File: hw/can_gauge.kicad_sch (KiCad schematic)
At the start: 9 parts, among them U2 MCP2515-xP

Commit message: hw: power and ground
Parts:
- removed U2: MCP2515-xP, symbol CAN:MCP2515-xP
- added C3, C4: 0.1 uF, symbol Device:C_Small
- added U1: MCP2515-xSO, Package_DIP:DIP-18_W7.62mm, symbol Interface_CAN_LIN:MCP2515-xSO
- renumbered Vreg to Vreg1
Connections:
- net +5V: now also UC1.1 (VDD), C3.1, C4.1, U1.18 (VDD)
- net GND: now also UC1.20 (VSS), C3.2, C4.2, U1.9 (VSS)
- net TX: now reaches XCVR1.1 (TXD)
- net TX: now also U1.1 (TXCAN)
- net RX: now reaches XCVR1.4 (RXD)
- net RX: now also U1.2 (RXCAN)
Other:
- moved on the sheet: UC1

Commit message: hw: mcp2515 serial lines
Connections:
- net at UC1.10 (RB7): now also U1.15 (SO)
- net at UC1.11 (RB6): now also U1.16 (~{CS})
- net at UC1.12 (RB5): now also U1.13 (SCK)
- net at UC1.13 (RB4): now also U1.14 (SI)
- net INT: now reaches UC1.17 (RA2)
- net INT: now also U1.12 (~{INT})
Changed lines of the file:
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@@
+	(wire
+		(pts
+			(xy 185.42 68.58) (xy 184.15 68.58)
+		)
+		(stroke
+			(width 0)
+			(type default)
+		)
+	)
 	(wire
 		(pts
@@
 	(wire
 		(pts
+			(xy 77.47 55.88) (xy 88.9 55.88)
+		)
+		(stroke
+			(width 0)
+			(type default)
+		)
+	)
+	(wire
+		(pts
 			(xy 232.41 36.83) (xy 236.22 36.83)
 		)
@@
 	(wire
 		(pts
+			(xy 77.47 99.06) (xy 77.47 55.88)
+		)
+		(stroke
+			(width 0)
+			(type default)
+		)
+	)
+	(wire
+		(pts
 			(xy 238.76 52.07) (xy 245.11 52.07)
 		)
@@
 	(wire
 		(pts
+			(xy 137.16 99.06) (xy 77.47 99.06)
+		)
+		(stroke
+			(width 0)
+			(type default)
+		)
+	)
+	(wire
+		(pts
 			(xy 104.14 31.75) (xy 104.14 38.1)
 		)
@@
 	(wire
 		(pts
+			(xy 153.67 60.96) (xy 137.16 60.96)
+		)
+		(stroke
+			(width 0)
+			(type default)
+		)
+	)
+	(wire
+		(pts
+			(xy 82.55 21.59) (xy 82.55 53.34)
+		)
+		(stroke
+			(width 0)
+			(type default)
+		)
+	)
+	(wire
+		(pts
 			(xy 177.8 39.37) (xy 181.61 39.37)
 		)
@@
 	(wire
 		(pts
+			(xy 153.67 55.88) (xy 132.08 55.88)
+		)
+		(stroke
+			(width 0)
+			(type default)
+		)
+	)
+	(wire
+		(pts
 			(xy 245.11 57.15) (xy 252.73 57.15)
 		)
@@
 	(wire
 		(pts
+			(xy 134.62 58.42) (xy 134.62 96.52)
+		)
+		(stroke
+			(width 0)
+			(type default)
+		)
+	)
+	(wire
+		(pts
 			(xy 236.22 59.69) (xy 238.76 59.69)
 		)
@@
 	(wire
 		(pts
+			(xy 132.08 93.98) (xy 82.55 93.98)
+		)
+		(stroke
+			(width 0)
+			(type default)
+		)
+	)
+	(wire
+		(pts
+			(xy 82.55 53.34) (xy 88.9 53.34)
+		)
+		(stroke
+			(width 0)
+			(type default)
+		)
+	)
+	(wire
+		(pts
 			(xy 113.03 38.1) (xy 118.11 38.1)
 		)
@@
 	(wire
 		(pts
+			(xy 153.67 53.34) (xy 132.08 53.34)
+		)
+		(stroke
+			(width 0)
+			(type default)
+		)
+	)
+	(wire
+		(pts
+			(xy 82.55 60.96) (xy 88.9 60.96)
+		)
+		(stroke
+			(width 0)
+			(type default)
+		)
+	)
+	(wire
+		(pts
+			(xy 82.55 93.98) (xy 82.55 60.96)
+		)
+		(stroke
+			(width 0)
+			(type default)
+		)
+	)
+	(wire
+		(pts
+			(xy 80.01 96.52) (xy 80.01 58.42)
+		)
+		(stroke
+			(width 0)
+			(type default)
+		)
+	)
+	(wire
+		(pts
+			(xy 132.08 21.59) (xy 82.55 21.59)
+		)
+		(stroke
+			(width 0)
+			(type default)
+		)
+	)
+	(wire
+		(pts
 			(xy 168.91 39.37) (xy 168.91 48.26)
 		)
@@
 	(wire
 		(pts
+			(xy 153.67 58.42) (xy 134.62 58.42)
+		)
+		(stroke
+			(width 0)
+			(type default)
+		)
+	)
+	(wire
+		(pts
 			(xy 208.28 62.23) (xy 210.82 62.23)
 		)
@@
 	(wire
 		(pts
+			(xy 132.08 53.34) (xy 132.08 21.59)
+		)
+		(stroke
+			(width 0)
+			(type default)
+		)
+	)
+	(wire
+		(pts
 			(xy 245.11 62.23) (xy 270.51 62.23)
 		)
@@
 	(wire
 		(pts
+			(xy 132.08 55.88) (xy 132.08 93.98)
+		)
+		(stroke
+			(width 0)
+			(type default)
+		)
+	)
+	(wire
+		(pts
 			(xy 238.76 62.23) (xy 245.11 62.23)
 		)
@@
 	(wire
 		(pts
+			(xy 134.62 96.52) (xy 80.01 96.52)
+		)
+		(stroke
+			(width 0)
+			(type default)
+		)
+	)
+	(wire
+		(pts
 			(xy 223.52 33.02) (xy 223.52 36.83)
 		)
@@
 		(pts
 			(xy 104.14 38.1) (xy 107.95 38.1)
+		)
+		(stroke
+			(width 0)
+			(type default)
+		)
+	)
+	(wire
+		(pts
+			(xy 80.01 58.42) (xy 88.9 58.42)
+		)
+		(stroke
+			(width 0)
+			(type default)
+		)
+	)
+	(wire
+		(pts
+			(xy 137.16 60.96) (xy 137.16 99.06)
 		)
 		(stroke
@@
 		)
 	)
+	(global_label "INT"
+		(shape input)
+		(at 88.9 71.12 180)
+		(fields_autoplaced yes)
+		(effects
+			(font
+				(size 1.27 1.27)
+			)
+			(justify right)
+		)
+		(property "Intersheetrefs" "${INTERSHEET_REFS}"
+			(at 83.0119 71.12 0)
+			(effects
+				(font
+					(size 1.27 1.27)
+				)
+				(justify right)
+				(hide yes)
+			)
+		)
+	)
 	(global_label "RX"
 		(shape input)
@@
 			(effects
 				(font
+					(size 1.27 1.27)
+				)
+				(justify left)
+				(hide yes)
+			)
+		)
+	)
+	(global_label "INT"
+		(shape output)
+		(at 185.42 68.58 0)
+		(fields_autoplaced yes)
+		(effects
+			(font
+				(size 1.27 1.27)
+			)
+			(justify left)
+		)
+		(property "Intersheetrefs" "${INTERSHEET_REFS}"
+			(at 191.3081 68.58 0)
+			(effects
+				(font

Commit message: hw: mcp2515 reset
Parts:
- added R4: 10k, symbol Device:R_Small_US
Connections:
- net +5V: now also R4.2
- net at U1.17 (~{RESET}): now also R4.1
- no-connect marks 0 -> 5
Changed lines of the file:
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@@
 		(color 0 0 0 0)
 	)
+	(no_connect
+		(at 184.15 76.2)
+	)
+	(no_connect
+		(at 184.15 81.28)
+	)
+	(no_connect
+		(at 184.15 73.66)
+	)
+	(no_connect
+		(at 184.15 71.12)
+	)
+	(no_connect
+		(at 184.15 78.74)
+	)
 	(wire
 		(pts
@@
 	(wire
 		(pts
+			(xy 195.58 83.82) (xy 195.58 82.55)
+		)
+		(stroke
+			(width 0)
+			(type default)
+		)
+	)
+	(wire
+		(pts
 			(xy 236.22 54.61) (xy 238.76 54.61)
 		)
@@
 	(wire
 		(pts
+			(xy 191.77 83.82) (xy 195.58 83.82)
+		)
+		(stroke
+			(width 0)
+			(type default)
+		)
+	)
+	(wire
+		(pts
 			(xy 245.11 62.23) (xy 270.51 62.23)
 		)
@@
 		(pts
 			(xy 104.14 38.1) (xy 104.14 48.26)
+		)
+		(stroke
+			(width 0)
+			(type default)
+		)
+	)
+	(wire
+		(pts
+			(xy 184.15 83.82) (xy 186.69 83.82)
 		)
 		(stroke
@@
 	)
 	(symbol
+		(lib_id "Device:R_Small_US")
+		(at 189.23 83.82 90)
+		(unit 1)
+		(exclude_from_sim no)
+		(in_bom yes)
+		(on_board yes)
+		(dnp no)
+		(fields_autoplaced yes)
+		(property "Reference" "R4"
+			(at 189.23 77.47 90)
+			(effects
+				(font
+					(size 1.27 1.27)
+				)
+			)
+		)
+		(property "Value" "10k"
+			(at 189.23 80.01 90)
+			(effects
+				(font
+					(size 1.27 1.27)
+				)
+			)
+		)
+		(property "Footprint" ""
+			(at 189.23 83.82 0)
+			(effects
+				(font
+					(size 1.27 1.27)
+				)
+				(hide yes)
+			)
+		)
+		(property "Datasheet" "~"
+			(at 189.23 83.82 0)
+			(effects
+				(font
+					(size 1.27 1.27)
+				)
+				(hide yes)
+			)
+		)
+		(property "Description" "Resistor, small US symbol"
+			(at 189.23 83.82 0)
+			(effects
+				(font
+					(size 1.27 1.27)
+				)
+				(hide yes)
+			)
+		)
+		(pin "2"
+		)
+		(pin "1"
+		)
+		(instances
+			(project ""
+				(path "/a1545928-1195-40b9-b3c4-78f837012afb"
+					(reference "R4")
+					(unit 1)
+				)
+			)
+		)
+	)
+	(symbol
 		(lib_id "power:GND")
 		(at 257.81 57.15 90)
@@
 					(unit 1)
 				)
+			)
+		)
+	)
+	(symbol
+		(lib_name "+5V_3")
+		(lib_id "power:+5V")
+		(at 195.58 82.55 0)
+		(unit 1)
+		(exclude_from_sim no)
+		(in_bom yes)
+		(on_board yes)
+		(dnp no)
+		(fields_autoplaced yes)
+		(property "Reference" "#PWR07"
+			(at 195.58 86.36 0)
+			(effects
+				(font
+					(size 1.27 1.27)
+				)
+				(hide yes)
+			)
+		)
+		(property "Value" "+5V"
+			(at 195.58 77.47 0)
+			(effects
+				(font
+					(size 1.27 1.27)
+				)
+			)
+		)
+		(property "Footprint" ""
+			(at 195.58 82.55 0)
+			(effects
+				(font
+					(size 1.27 1.27)
+				)
+				(hide yes)
+			)
+		)
+		(property "Datasheet" ""
+			(at 195.58 82.55 0)
+			(effects
+				(font
+					(size 1.27 1.27)
+				)
+				(hide yes)
+			)
+		)
+		(property "Description" "Power symbol creates a global label with name \"+5V\""
+			(at 195.58 82.55 0)
+			(effects
+				(font
+					(size 1.27 1.27)
+				)
+				(hide yes)
+			)
+		)
+		(pin "1"
+		)
+		(instances
+			(project ""
+				(path "/a1545928-1195-40b9-b3c4-78f837012afb"
+					(reference "#PWR07")
+					(unit 1)
+				)

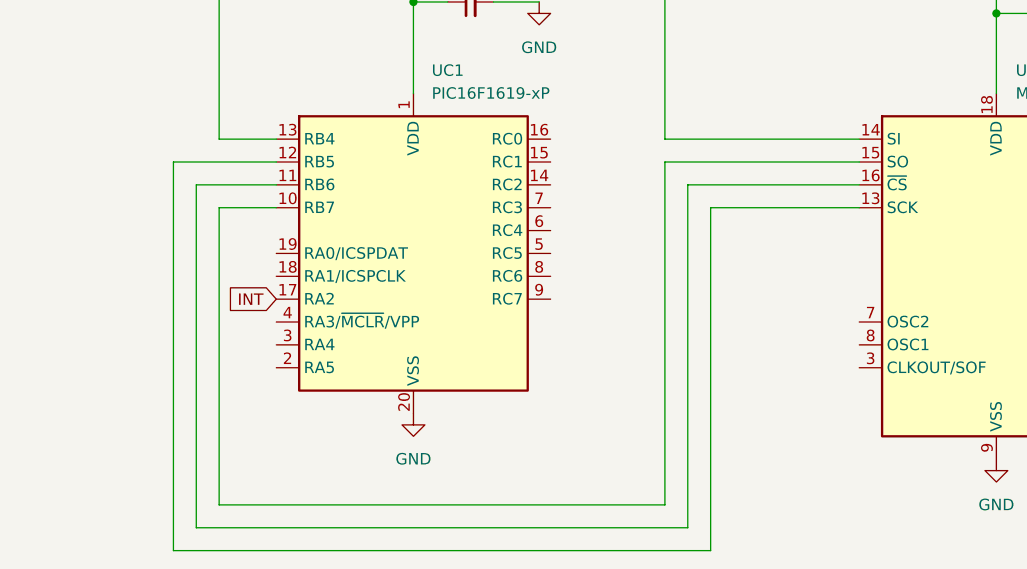
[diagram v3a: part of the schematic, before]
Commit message: hw: pic/mcp clock line
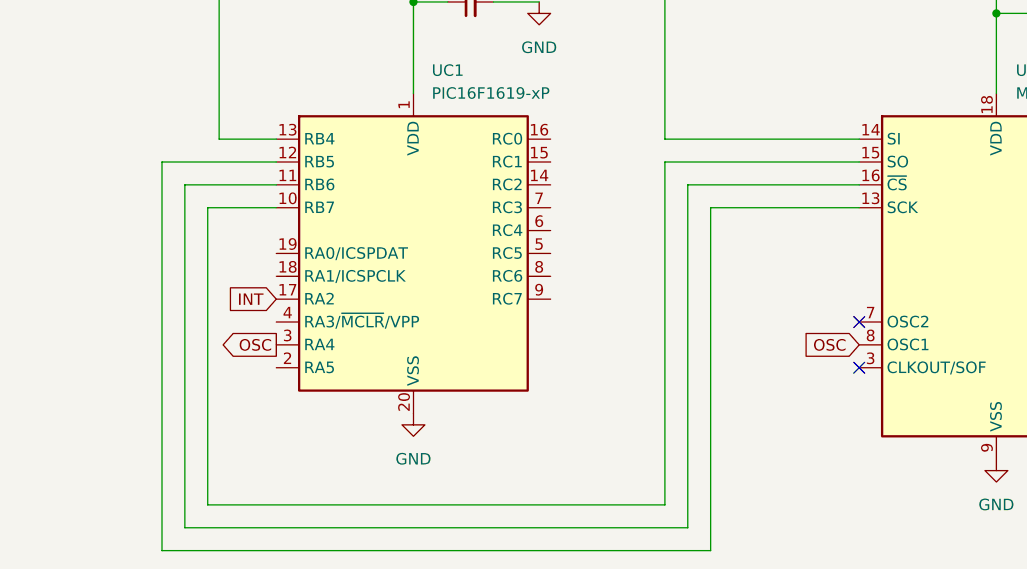
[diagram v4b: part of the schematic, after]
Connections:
- net OSC: now reaches UC1.3 (RA4)
- net OSC: now also U1.8 (OSC1)
- no-connect marks 5 -> 7
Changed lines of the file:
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@@
+	)
+	(no_connect
+		(at 153.67 78.74)
 	)
 	(no_connect
@@
 	)
 	(no_connect
+		(at 153.67 73.66)
+	)
+	(no_connect
 		(at 184.15 78.74)
 	)
@@
 	(wire
 		(pts
-			(xy 77.47 55.88) (xy 88.9 55.88)
+			(xy 76.2 55.88) (xy 88.9 55.88)
 		)
 		(stroke
@@
 	(wire
 		(pts
-			(xy 77.47 99.06) (xy 77.47 55.88)
+			(xy 76.2 99.06) (xy 76.2 55.88)
 		)
 		(stroke
@@
 	(wire
 		(pts
-			(xy 137.16 99.06) (xy 77.47 99.06)
+			(xy 137.16 99.06) (xy 76.2 99.06)
 		)
 		(stroke
@@
 	(wire
 		(pts
-			(xy 132.08 93.98) (xy 82.55 93.98)
+			(xy 132.08 93.98) (xy 81.28 93.98)
 		)
 		(stroke
@@
 	(wire
 		(pts
-			(xy 82.55 60.96) (xy 88.9 60.96)
-		)
-		(stroke
-			(width 0)
-			(type default)
-		)
-	)
-	(wire
-		(pts
-			(xy 82.55 93.98) (xy 82.55 60.96)
-		)
-		(stroke
-			(width 0)
-			(type default)
-		)
-	)
-	(wire
-		(pts
-			(xy 80.01 96.52) (xy 80.01 58.42)
+			(xy 81.28 60.96) (xy 88.9 60.96)
+		)
+		(stroke
+			(width 0)
+			(type default)
+		)
+	)
+	(wire
+		(pts
+			(xy 81.28 93.98) (xy 81.28 60.96)
+		)
+		(stroke
+			(width 0)
+			(type default)
+		)
+	)
+	(wire
+		(pts
+			(xy 78.74 96.52) (xy 78.74 58.42)
 		)
 		(stroke
@@
 	(wire
 		(pts
-			(xy 134.62 96.52) (xy 80.01 96.52)
+			(xy 134.62 96.52) (xy 78.74 96.52)
 		)
 		(stroke
@@
 	(wire
 		(pts
-			(xy 80.01 58.42) (xy 88.9 58.42)
+			(xy 78.74 58.42) (xy 88.9 58.42)
 		)
 		(stroke
@@
 		)
 	)
+	(global_label "OSC"
+		(shape input)
+		(at 153.67 76.2 180)
+		(fields_autoplaced yes)
+		(effects
+			(font
+				(size 1.27 1.27)
+			)
+			(justify right)
+		)
+		(property "Intersheetrefs" "${INTERSHEET_REFS}"
+			(at 146.8748 76.2 0)
+			(effects
+				(font
+					(size 1.27 1.27)
+				)
+				(justify right)
+				(hide yes)
+			)
+		)
+	)
 	(global_label "INT"
 		(shape input)
@@
 				(hide yes)
 			)
+		)
+	)
+	(global_label "OSC"
+		(shape output)
+		(at 88.9 76.2 180)
+		(fields_autoplaced yes)
+		(effects
+			(font
+				(size 1.27 1.27)
+			)
+			(justify right)
+		)
+		(property "Intersheetrefs" "${INTERSHEET_REFS}"
+			(at 82.1048 76.2 0)
+			(effects
+				(font
+					(size 1.27 1.27)
+				)
+				(justify right)
+				(hide yes)
+			)

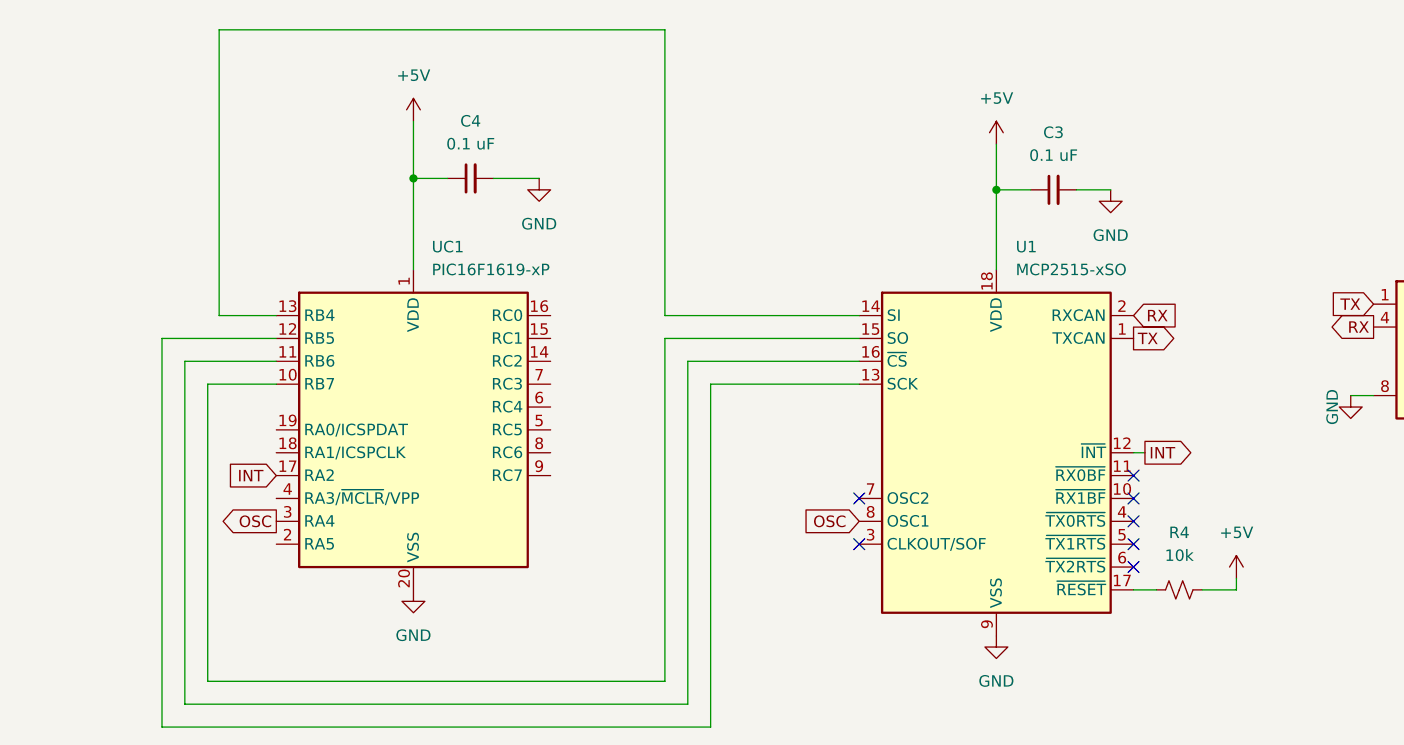
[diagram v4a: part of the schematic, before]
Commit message: hw: serial line labels
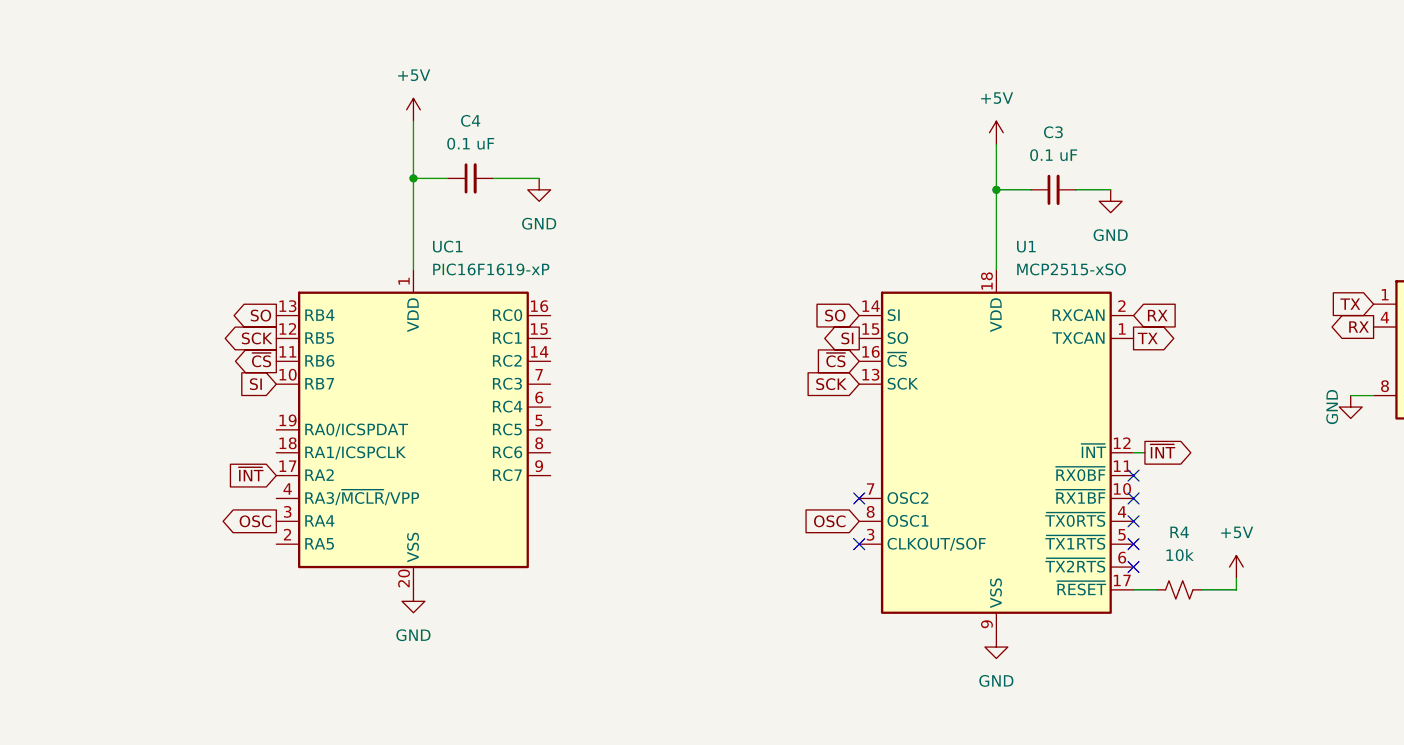
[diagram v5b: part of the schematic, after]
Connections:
- net SI: now reaches U1.15 (SO), UC1.10 (RB7)
- net ~{CS}: now reaches U1.16 (~{CS}), UC1.11 (RB6)
- net SCK: now reaches U1.13 (SCK), UC1.12 (RB5)
- net SO: now reaches U1.14 (SI), UC1.13 (RB4)
- net INT renamed ~{INT}

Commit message: hw: connector
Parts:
- added J1: (no value), symbol Connector:DIN41612_02x16_AB
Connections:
- net +12V: now also J1.a1 (Pin_a1)
- net CAN_H: now also J1.a11 (Pin_a11)
- net CAN_L: now also J1.a12 (Pin_a12)
- net GND: now also J1.a2 (Pin_a2)
- new net M1P1: J1.b1 (Pin_b1)
- new net M1P2: J1.b2 (Pin_b2)
- new net M1P3: J1.b3 (Pin_b3)
- new net M1P4: J1.b4 (Pin_b4)
- new net M2P1: J1.b5 (Pin_b5)
- new net M2P2: J1.b6 (Pin_b6)
- new net M2P3: J1.b7 (Pin_b7)
- new net M2P4: J1.b8 (Pin_b8)
- new net M3P1: J1.b9 (Pin_b9)
- new net M3P2: J1.b10 (Pin_b10)
- new net M3P3: J1.b11 (Pin_b11)
- new net M3P4: J1.b12 (Pin_b12)
- new net M4P1: J1.a10 (Pin_a10)
- new net M4P2: J1.a9 (Pin_a9)
- new net M4P3: J1.a8 (Pin_a8)
- new net M4P4: J1.a7 (Pin_a7)
- new net M5P1: J1.a6 (Pin_a6)
- new net M5P2: J1.a5 (Pin_a5)
- new net M5P3: J1.a4 (Pin_a4)
- new net M5P4: J1.a3 (Pin_a3)
